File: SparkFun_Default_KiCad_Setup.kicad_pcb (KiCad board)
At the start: 4 copper layers, 50.8 x 50.8 mm, 18 parts, among them U2 RT9080-3.3

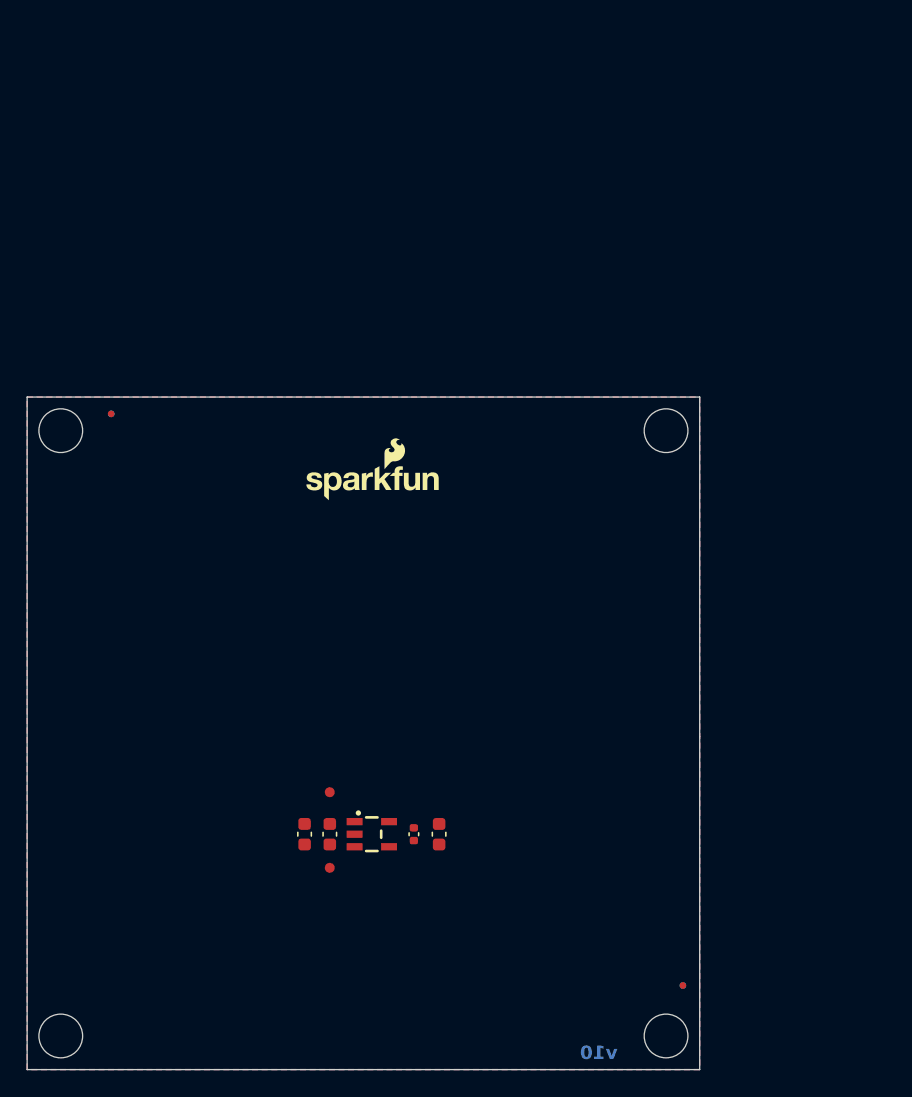
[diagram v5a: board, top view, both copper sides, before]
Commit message: Change page size and board origin
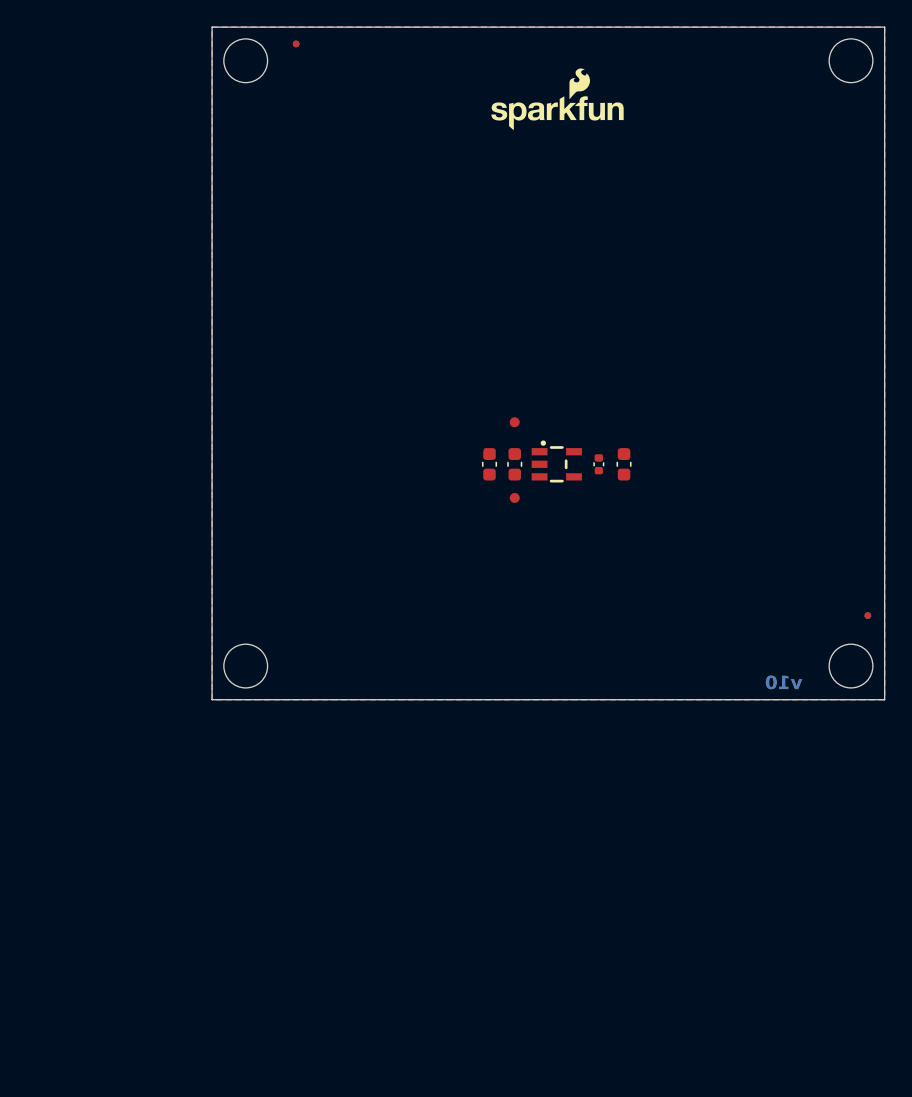
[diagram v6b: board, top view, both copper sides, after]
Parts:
- moved FID2 31.2 mm to (165.1, 118.1)
- moved FID4 31.2 mm to (165.1, 118.1)
- moved ST2 31.2 mm to (118.1, 121.9)
- moved ST4 31.2 mm to (163.8, 121.9)
- moved C3 31.2 mm to (138.4, 106.7)
- moved TP1 31.2 mm to (138.4, 109.2)
- moved TP2 31.2 mm to (138.4, 103.5)
- moved C2 31.2 mm to (136.5, 106.7)
- moved C4 31.2 mm to (144.8, 106.7)
- moved C5 31.2 mm to (146.7, 106.7)
- moved FID1 31.2 mm to (121.9, 74.9)
- moved FID3 31.2 mm to (121.9, 74.9)
- moved ST1 31.2 mm to (118.1, 76.2)
- moved ST3 31.2 mm to (163.8, 76.2)
- moved G*** 31.2 mm to (141.6, 80.0)
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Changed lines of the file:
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@@
     (thickness 1.6)
   )
-  (paper "A4")
+  (paper "USLetter")
   (title_block
     (comment 1 "Designed by: You")
@@
     )
     (pad_to_mask_clearance 0)
-    (aux_axis_origin 101.6 152.4)
-    (grid_origin 101.6 152.4)
+    (aux_axis_origin 115.57 124.46)
+    (grid_origin 115.57 124.46)
     (pcbplotparams
       (layerselection 0x00010fc_ffffffff)
@@
   (net 4 "unconnected-(U2-NC-Pad4)")
   (footprint "SparkFun-Aesthetic:Creative_Commons_License" (layer "F.Cu")
-    (at 231.775 163.195)
+    (at 215.265 168.91)
     (tags "Creative Commons License")
     (property "Sheetfile" "SparkFun_Default_KiCad_Setup.kicad_sch")
@@
   )
   (footprint "SparkFun-Semiconductor-Standard:SOT23-5" (layer "F.Cu")
-    (at 127.635 134.62)
+    (at 141.605 106.68)
     (property "Imax" "600mA")
     (property "Iq" "4µA")
@@
   )
   (footprint "SparkFun-Connector:TestPoint-0.75mm" (layer "F.Cu")
-    (at 124.46 131.445)
+    (at 138.43 103.505)
     (property "Sheetfile" "SparkFun_Default_KiCad_Setup.kicad_sch")
     (property "Sheetname" "")
@@
   )
   (footprint "SparkFun-Hardware:Standoff" (layer "F.Cu")
-    (at 149.86 149.86)
+    (at 163.83 121.92)
     (property "Sheetfile" "SparkFun_Default_KiCad_Setup.kicad_sch")
     (property "Sheetname" "")
@@
   )
   (footprint "SparkFun-Aesthetic:Fiducial_0.5mm_Mask1mm" (layer "F.Cu")
-    (at 151.13 146.05)
+    (at 165.1 118.11)
     (descr "Circular Fiducial, 0.5mm bare copper, 1mm soldermask opening (Level C)")
     (tags "fiducial")
@@
   )
   (footprint "SparkFun-Aesthetic:Fiducial_0.5mm_Mask1mm" (layer "F.Cu")
-    (at 107.95 102.87)
+    (at 121.92 74.93)
     (descr "Circular Fiducial, 0.5mm bare copper, 1mm soldermask opening (Level C)")
     (tags "fiducial")
@@
   )
   (footprint "SparkFun-Capacitor:C_0603_1608Metric" (layer "F.Cu")
-    (at 124.46 134.62 -90)
+    (at 138.43 106.68 -90)
     (tags "capacitor")
     (property "PROD_ID" "CAP-13930")
@@
   )
   (footprint "SparkFun-Hardware:Standoff" (layer "F.Cu")
-    (at 149.86 104.14)
+    (at 163.83 76.2)
     (property "Sheetfile" "SparkFun_Default_KiCad_Setup.kicad_sch")
     (property "Sheetname" "")
@@
   )
   (footprint "SparkFun-Aesthetic:SparkFun_Logo_10mm" (layer "F.Cu")
-    (at 127.635 107.95)
+    (at 141.605 80.01)
     (attr board_only exclude_from_pos_files exclude_from_bom)
     (fp_text reference "G***" (at 0 -3.8) (layer "F.Fab")
@@
   )
   (footprint "SparkFun-Capacitor:C_0603_1608Metric" (layer "F.Cu")
-    (at 132.715 134.62 -90)
+    (at 146.685 106.68 -90)
     (tags "capacitor")
     (property "PROD_ID" "CAP-11015")
@@
   )
   (footprint "SparkFun-Connector:TestPoint-0.75mm" (layer "F.Cu")
-    (at 124.46 137.16)
+    (at 138.43 109.22)
     (property "Sheetfile" "SparkFun_Default_KiCad_Setup.kicad_sch")
     (property "Sheetname" "")
@@
   )
   (footprint "SparkFun-Capacitor:C_0603_1608Metric" (layer "F.Cu")
-    (at 122.555 134.62 -90)
+    (at 136.525 106.68 -90)
     (tags "capacitor")
     (property "PROD_ID" "CAP-20155")
@@
   )
   (footprint "SparkFun-Hardware:Standoff" (layer "F.Cu")
-    (at 104.14 104.14)
+    (at 118.11 76.2)
     (property "Sheetfile" "SparkFun_Default_KiCad_Setup.kicad_sch")
     (property "Sheetname" "")
@@
   )
   (footprint "SparkFun-Capacitor:C_0402_1005Metric" (layer "F.Cu")
-    (at 130.81 134.62 -90)
+    (at 144.78 106.68 -90)
     (descr "Capacitor SMD 0402 (1005 Metric), square (rectangular) end terminal, IPC_7351 nominal, (Body size source: IPC-SM-782 page 76, https://www.pcb-3d.com/wordpress/wp-content/uploads/ipc-sm-782a_amendment_1_and_2.pdf), generated with kicad-footprint-generator")
     (tags "capacitor")
@@
   )
   (footprint "SparkFun-Hardware:Standoff" (layer "F.Cu")
-    (at 104.14 149.86)
+    (at 118.11 121.92)
     (property "Sheetfile" "SparkFun_Default_KiCad_Setup.kicad_sch")
     (property "Sheetname" "")
@@
   )
   (footprint "SparkFun-Aesthetic:Fiducial_0.5mm_Mask1mm" (layer "B.Cu")
-    (at 107.95 102.87 180)
+    (at 121.92 74.93 180)
     (descr "Circular Fiducial, 0.5mm bare copper, 1mm soldermask opening (Level C)")
     (tags "fiducial")
@@
   )
   (footprint "SparkFun-Aesthetic:Fiducial_0.5mm_Mask1mm" (layer "B.Cu")
-    (at 151.13 146.05 180)
+    (at 165.1 118.11 180)
     (descr "Circular Fiducial, 0.5mm bare copper, 1mm soldermask opening (Level C)")
     (tags "fiducial")
@@
   (gr_poly
     (pts
-      (xy 101.6 152.4)
-      (xy 101.6 101.6)
-      (xy 152.4 101.6)
-      (xy 152.4 127.254)
-      (xy 152.4 135.636)
-      (xy 152.4 152.4)
+      (xy 115.57 124.46)
+      (xy 115.57 73.66)
+      (xy 166.37 73.66)
+      (xy 166.37 99.314)
+      (xy 166.37 107.696)
+      (xy 166.37 124.46)
     )
     (stroke (width 0.1) (type solid)) (fill none) (layer "Edge.Cuts"))
-  (gr_text "v10" (at 144.78 151.13) (layer "B.Cu" knockout)
+  (gr_text "v10" (at 158.75 123.19) (layer "B.Cu" knockout)
     (effects (font (size 1.016 1.016) (thickness 0.254) bold) (justify mirror))
   )
-  (gr_text "No Clean Process" (at 241.935 176.53) (layer "F.Fab")
+  (gr_text "No Clean Process" (at 226.06 182.88) (layer "F.Fab")
     (effects (font (size 1.27 1.27) (thickness 0.15)) (justify left bottom))
   )
-  (gr_text "Inner Copper Weight: 0.5oz" (at 241.935 180.34) (layer "F.Fab")
+  (gr_text "Inner Copper Weight: 0.5oz" (at 226.06 186.69) (layer "F.Fab")
     (effects (font (size 1.27 1.27) (thickness 0.15)) (justify left bottom))
   )
-  (gr_text "Layers: 4" (at 211.405892 176.53) (layer "F.Fab")
+  (gr_text "Layers: 4" (at 195.530892 182.88) (layer "F.Fab")
     (effects (font (size 1.27 1.27) (thickness 0.15)) (justify left bottom))
   )
-  (gr_text "Silkscreen Color: White" (at 211.455 174.625) (layer "F.Fab")
+  (gr_text "Silkscreen Color: White" (at 195.58 180.975) (layer "F.Fab")
     (effects (font (size 1.27 1.27) (thickness 0.15)) (justify left bottom))
   )
-  (gr_text "Solder Mask: Red" (at 211.455 172.72) (layer "F.Fab")
+  (gr_text "Solder Mask: Red" (at 195.58 179.07) (layer "F.Fab")
     (effects (font (size 1.27 1.27) (thickness 0.15)) (justify left bottom))
   )
-  (gr_text "Material: TG155" (at 241.935 174.625) (layer "F.Fab")
+  (gr_text "Material: TG155" (at 226.06 180.975) (layer "F.Fab")
     (effects (font (size 1.27 1.27) (thickness 0.15)) (justify left bottom))
   )
-  (gr_text "Controlled Impedance: JLC7628" (at 241.935 172.72) (layer "F.Fab")
+  (gr_text "Controlled Impedance: JLC7628" (at 226.06 179.07) (layer "F.Fab")
     (effects (font (size 1.27 1.27) (thickness 0.15)) (justify left bottom))
   )
-  (gr_text "Outer Copper Weight: 1oz" (at 241.935 178.435) (layer "F.Fab")
+  (gr_text "Outer Copper Weight: 1oz" (at 226.06 184.785) (layer "F.Fab")
     (effects (font (size 1.27 1.27) (thickness 0.15)) (justify left bottom))
   )
-  (gr_text "Thickness: 1.6mm" (at 211.455 178.435) (layer "F.Fab")
+  (gr_text "Thickness: 1.6mm" (at 195.58 184.785) (layer "F.Fab")
     (effects (font (size 1.27 1.27) (thickness 0.15)) (justify left bottom))
   )
-  (gr_text "Finish: ENIG" (at 211.455 180.34) (layer "F.Fab")
+  (gr_text "Finish: ENIG" (at 195.58 186.69) (layer "F.Fab")
     (effects (font (size 1.27 1.27) (thickness 0.15)) (justify left bottom))
   )
-  (gr_text "Ordering Notes" (at 205.105 169.545) (layer "F.Fab")
+  (gr_text "Ordering Notes" (at 189.23 175.895) (layer "F.Fab")
     (effects (font (size 2 2) (thickness 0.15)) (justify left bottom))
   )
   (dimension (type aligned) (layer "Dwgs.User")
-    (pts (xy 101.6 101.6) (xy 152.4 101.6))
+    (pts (xy 115.57 73.66) (xy 166.37 73.66))
     (height -3.81)
-    (gr_text "50.8 mm" (at 127 96.64) (layer "Dwgs.User")
+    (gr_text "2000 mils" (at 140.97 68.7) (layer "Dwgs.User")
       (effects (font (size 1 1) (thickness 0.15)))
     )
@@
   )
   (dimension (type aligned) (layer "Dwgs.User")
-    (pts (xy 152.4 152.4) (xy 152.4 149.86))
+    (pts (xy 166.37 124.46) (xy 166.37 121.92))
     (height 2.54)
-    (gr_text "2.5 mm" (at 153.79 151.13 90) (layer "Dwgs.User")
+    (gr_text "100 mils" (at 167.76 123.19 90) (layer "Dwgs.User")
       (effects (font (size 1 1) (thickness 0.15)))
     )
@@
   )
   (dimension (type aligned) (layer "Dwgs.User")
-    (pts (xy 101.6 152.4) (xy 104.14 152.4))
+    (pts (xy 115.57 124.46) (xy 118.11 124.46))
     (height 2.54)
-    (gr_text "2.5 mm" (at 102.87 153.79) (layer "Dwgs.User")
+    (gr_text "100 mils" (at 116.84 125.85) (layer "Dwgs.User")
       (effects (font (size 1 1) (thickness 0.15)))
     )
@@
   )
   (dimension (type aligned) (layer "Dwgs.User")
-    (pts (xy 101.6 152.4) (xy 101.6 101.6))
+    (pts (xy 115.57 124.46) (xy 115.57 73.66))
     (height -3.81)
-    (gr_text "50.8 mm" (at 96.64 127 90) (layer "Dwgs.User")
+    (gr_text "2000 mils" (at 110.61 99.06 90) (layer "Dwgs.User")
       (effects (font (size 1 1) (thickness 0.15)))
     )
@@
     (polygon
       (pts
-        (xy 101.6 152.4)
-        (xy 101.6 101.6)
-        (xy 152.4 101.6)
-        (xy 152.4 152.4)
+        (xy 115.57 124.46)
+        (xy 115.57 73.66)
+        (xy 166.37 73.66)
+        (xy 166.37 124.46)
       )
     )
